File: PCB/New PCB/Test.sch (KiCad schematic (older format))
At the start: 52 parts, among them P10 CONN_2, P11 CONN_2, P12 CONN_1, P13 CONN_1, P14 CONN_1, P15 CONN_1, P16 CONN_6, P17 CONN_1, P18 CONN_1, P19 CONN_2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

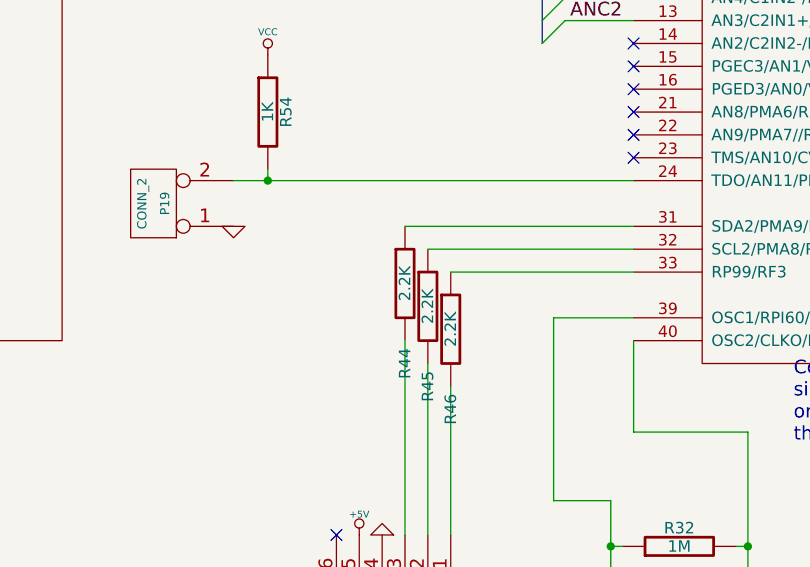
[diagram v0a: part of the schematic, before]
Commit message: Motor/Magnet PCB (KiCad)
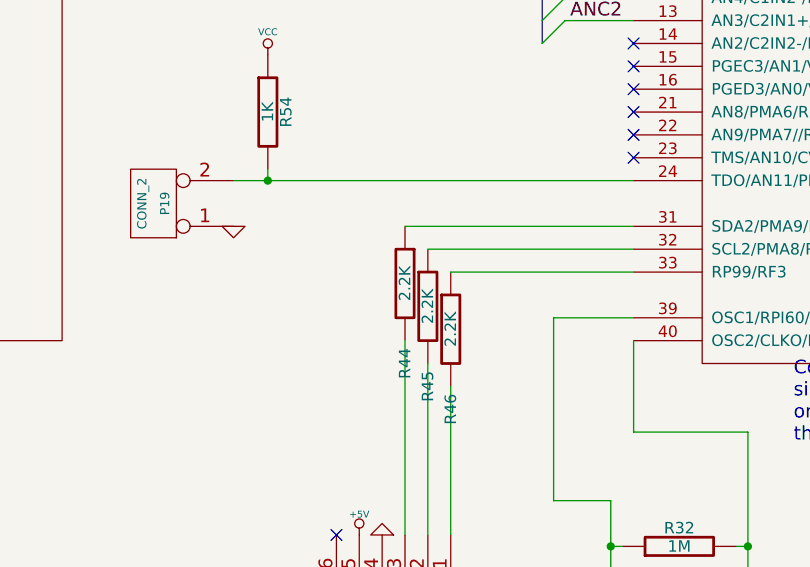
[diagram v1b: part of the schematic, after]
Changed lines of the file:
@@
 Sheet 1 4
 Title ""
-Date "5 jun 2013"
+Date "1 jul 2013"
 Rev ""
 Comp ""
@@
 F 3 "~" H 7100 9000 60  0000 C CNN
 	1    7100 9000
-	1    0    0    -1
-$EndComp
-$Comp
+	-1   0    0    -1
+$EndComp
+$Comp

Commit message: Fixes to Schematics
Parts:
- removed U1: DSPIC33EP512MC806, ~, symbol DSPIC33EP512MC806
- added U?: DSPIC33EP512MC806_JAKE, ~, symbol DSPIC33EP512MC806_JAKE
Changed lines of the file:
@@
 Sheet 1 4
 Title ""
-Date "8 jul 2013"
+Date "15 jul 2013"
 Rev ""
 Comp ""
@@
 Text Notes 9850 12650 0    200  ~ 0
 XBee Chip
-$Comp
-L DSPIC33EP512MC806 U1
-U 1 1 51A29A62
-P 10350 7500
-F 0 "U1" H 10200 9000 60  0000 C CNN
-F 1 "DSPIC33EP512MC806" H 10150 9150 60  0000 C CNN
-F 2 "~" H 10350 7500 60  0000 C CNN
-F 3 "~" H 10350 7500 60  0000 C CNN
-	1    10350 7500
-	1    0    0    -1
-$EndComp
 $Comp
 L XBEE-1B2 XBEE1
@@
 	1    0    0    -1
 $EndComp
+$Comp
+L DSPIC33EP512MC806_JAKE U?
+U 1 1 51E428F5
+P 10350 7500
+F 0 "U?" H 10350 7900 60  0000 C CNN
+F 1 "DSPIC33EP512MC806_JAKE" H 10400 8000 60  0000 C CNN
+F 2 "~" H 10350 7900 60  0000 C CNN
+F 3 "~" H 10350 7900 60  0000 C CNN
+	1    10350 7500
+	1    0    0    -1
+$EndComp
